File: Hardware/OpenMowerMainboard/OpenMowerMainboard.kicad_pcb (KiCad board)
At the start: 2 copper layers, 180 x 170 mm, 178 parts, among them IC1 74ALVC164245DGG,11, IC2 TSC101CILT, IC3 MAX20405AFOF_VY+T, J1 Conn_02x11_Top_Bottom, J10 Conn_01x05, J11 Conn_01x03_Male, J12 Conn_01x03_Male, J13 Conn_01x03_Male, J14 Conn_01x03_Male, J16 Conn_01x08, J17 Conn_01x02, J18 Conn_01x02, J19 Conn_01x04, J2 Conn_02x04_Top_Bottom, J20 Conn_01x10_Female, J21 Raspberry_Pi_2_3, J22 Conn_02x04_Odd_Even, J23 Conn_01x08, J3 Conn_01x02, J4 Conn_01x05, J5 Conn_01x04, J6 Conn_01x04, J7 Conn_01x04, J8 Conn_01x04, J9 Conn_01x04, M1 Fan, Q13 BSS138, Q14 BSS138, Q15 BSS138, Q16 BSS138, Q3 BSS138, Q5 BSS138, Q6 Q_PMOS_GDS, SW1 MK-11C04-G013, SW2 DA-01BP, U1 DNP, U10 74HC4051, U11 Pico, U2 MCP604, U3 SIP32509DT, U4 xESC2, U5 xESC2, U6 xESC2, U7 SN74LV1T34DBV, U9 74HC4051

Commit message: Initial mainboard for Worx Landroid WR105SI
Moved components and a few connectors around to make the mainboard fit
in the Worx Landroid WR105SI. No functional changes (hopefully).

Mounting holes are TBD.
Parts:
- removed H1: MountingHole_Pad, MountingHole:MountingHole_5mm_Pad_Via
- moved U1 160.3 mm to (187.9, 161.8), turned to 90 degrees
- moved LOGO1 160.1 mm to (163.5, 72.8)
- moved LOGO2 160.1 mm to (155.8, 72.5)
- moved H2 159.5 mm to (159.6, 94.7)
- moved J16 157.2 mm to (215.0, 69.4), turned to -90 degrees
- moved R7 152.0 mm to (212.7, 63.6)
- moved R13 147.8 mm to (210.1, 63.6)
- moved FID15 147.6 mm to (171.9, 165.3), turned to 90 degrees
- moved FID7 147.3 mm to (193.0, 138.8), turned to 90 degrees
- moved C10 147.0 mm to (183.0, 153.0), turned to -90 degrees
- moved J23 146.5 mm to (215.0, 75.0), turned to -90 degrees
- moved J20 140.6 mm to (198.1, 114.4), turned to 180 degrees
- moved D23 138.8 mm to (200.4, 83.8), turned to 0 degrees
- moved C19 138.0 mm to (188.4, 133.6), turned to 0 degrees
- moved C21 137.5 mm to (189.2, 131.2), turned to 0 degrees
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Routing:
- net /RobotConnectors/V_CHARGE: track 44.6 -> 267.5 mm
- net /RobotConnectors/V_BATTERY: track 31.3 -> 215.9 mm
- net /RobotConnectors/CHARGE_SHUNT_MINUS: track 82.0 -> 206.1 mm
- net /RobotConnectors/CHARGE_SHUNT_PLUS: track 80.0 -> 203.8 mm
- net /RobotConnectors/ENABLE_CHARGE: track 95.5 -> 216.1 mm, vias 2 -> 4
- net /ESCs/MR_TX: track 100.3 -> 194.9 mm
- net /ESCs/MR_RX: track 77.5 -> 171.2 mm
- net /pico/SOUND_BUSY: track 111.9 -> 24.4 mm, vias 3 -> 1
- net +5V: track 887.6 -> 970.6 mm, vias 18 -> 20
- net /IMU/SCK: track 205.5 -> 125.8 mm
- net /IMU/MOSI: track 202.0 -> 123.4 mm
- net /IMU/MISO: track 216.3 -> 138.8 mm
- net Net-(JP6-B): track 98.1 -> 169.3 mm, vias 5 -> 7
- net /IMU/~{CS}: track 186.9 -> 122.7 mm
- net /pico/SOUND_TX: track 107.9 -> 44.2 mm, vias 1 -> 3
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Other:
- board size 180 x 170 mm -> 257.1 x 170 mm

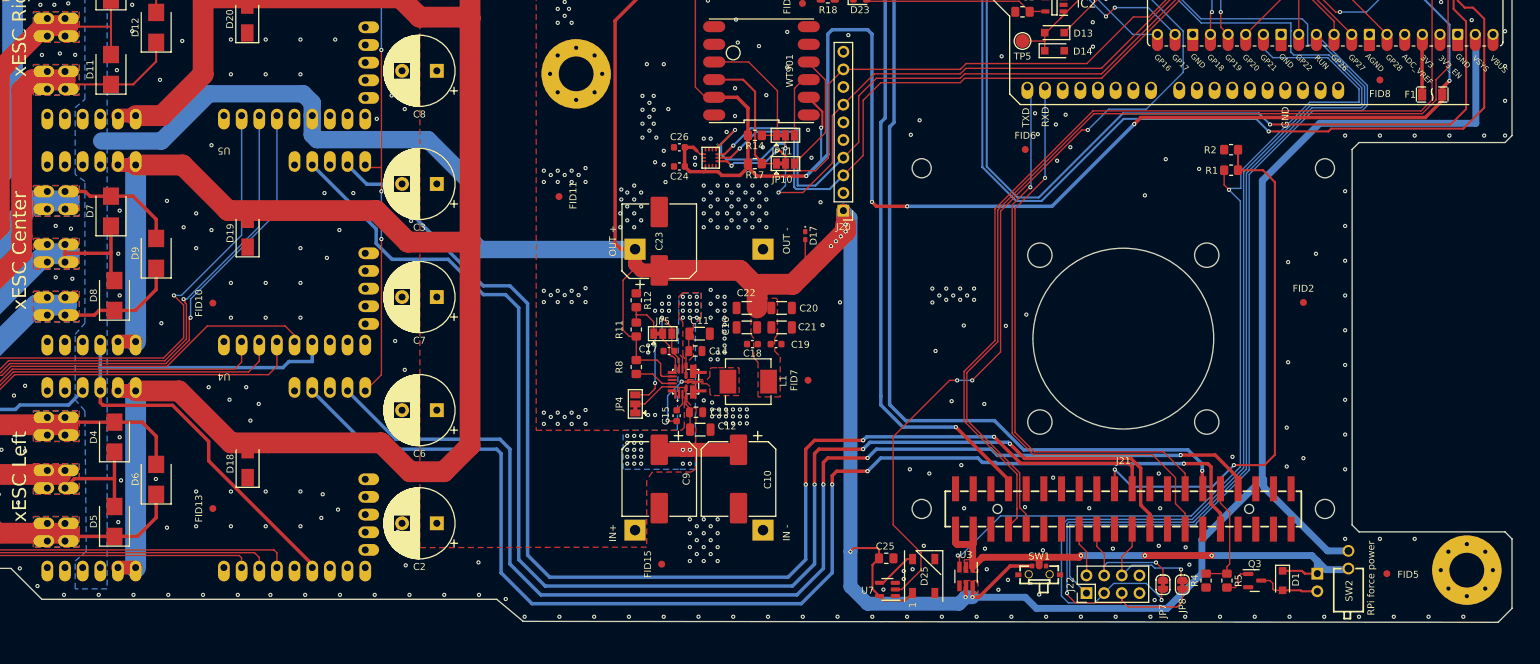
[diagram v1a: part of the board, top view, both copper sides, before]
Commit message: mainboard: squeeze bottom mid slightly
Slightly reduce board height near bottom mid. Should give a bit more
freedom when placing the board in the Landroid.
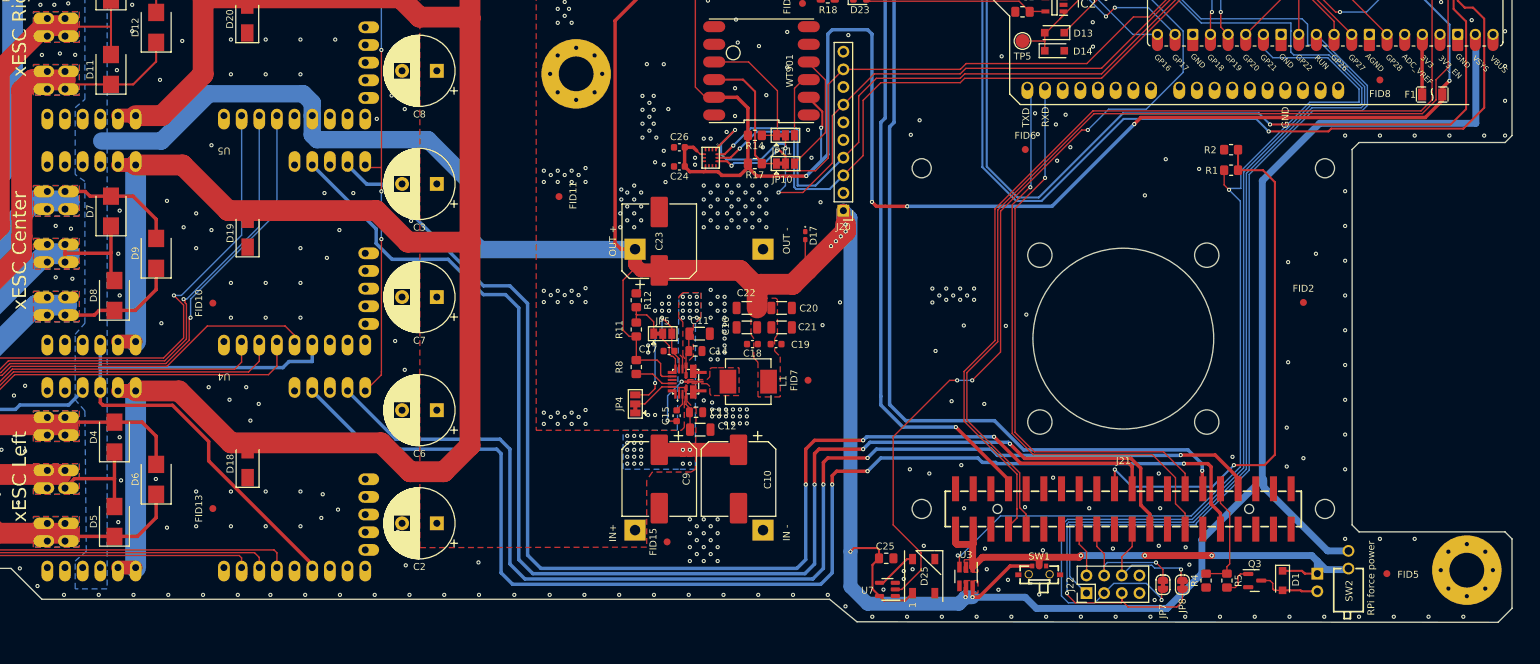
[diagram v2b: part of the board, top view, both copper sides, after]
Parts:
- moved FID15 3.30 mm to (172.7, 162.1)
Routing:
- net /ESCs/ML_RX: track 178.5 -> 176.2 mm
- net /ESCs/ML_TX: track 170.2 -> 168.3 mm
- net /ESCs/MC_RX: track 195.0 -> 193.5 mm
- net /ESCs/MC_TX: track 180.6 -> 179.6 mm
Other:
- outline, holes or cut-outs redrawn

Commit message: mainboard: no mounting holes, squeeze connectors
Remove mounting holes and squeeze upper right connectors
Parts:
- removed H2, H3, H4: MountingHole_Pad, MountingHole:MountingHole_5mm_Pad_Via
- moved FID11 27.3 mm to (171.0, 88.8)
- moved J5 12.7 mm to (266.7, 8.58)
- moved J6 12.7 mm to (266.7, 16.6)
- moved J11 10.8 mm to (282.1, 8.58)
- moved J12 10.8 mm to (282.1, 16.6)
- moved FID14 4.86 mm to (281.4, 24.4)
- moved C13 0.10 mm to (177.0, 143.4)
- moved C15 0.10 mm to (174.2, 143.9)
- moved C2 0.10 mm to (139.7, 159.3)
- moved C20 0.10 mm to (189.3, 128.4)
- moved C22 0.10 mm to (184.3, 128.4)
- moved D25 0.10 mm to (209.7, 166.9)
- moved J21 0.10 mm to (238.4, 157.3)
- moved JP7 0.10 mm to (244.1, 168.2)
- moved JP8 0.10 mm to (246.9, 168.2)
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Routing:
- net +5V: track 970.6 -> 1038.3 mm
- net /RobotConnectors/HALL_SWITCH_2_5V: track 50.3 -> 57.4 mm
- net /RobotConnectors/USS_3_ECHO_5V: track 50.6 -> 45.7 mm
- net /RobotConnectors/USS_4_ECHO_5V: track 42.5 -> 38.4 mm
- net /RobotConnectors/USS_5_ECHO_5V: track 34.9 -> 30.9 mm
- net /RobotConnectors/USS_2_TRIGGER_5V: track 68.7 -> 64.9 mm
- net /RobotConnectors/HALL_SWITCH_1_5V: track 62.1 -> 64.6 mm
- net /RobotConnectors/USS_1_TRIGGER_5V: track 77.4 -> 75.1 mm
- net /RobotConnectors/USS_1_ECHO_5V: track 65.5 -> 63.4 mm
- net /RobotConnectors/USS_2_ECHO_5V: track 57.5 -> 58.7 mm
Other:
- outline, holes or cut-outs redrawn

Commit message: mainboard: remove unused area in middle of board
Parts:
- moved LOGO2 55.5 mm to (167.4, 126.8), turned to 90 degrees
- moved LOGO1 47.6 mm to (167.6, 120.2), turned to -90 degrees
- moved FID13 18.3 mm to (125.2, 152.8)
- moved FID10 18.3 mm to (125.2, 123.3)
- moved FID12 18.3 mm to (90.2, 108.8)
- moved Q5 18.3 mm to (90.5, 75.2)
- moved D20 18.3 mm to (130.2, 82.5)
- moved Q6 18.3 mm to (86.5, 81.5)
- moved R26 18.3 mm to (95.5, 75.2)
- moved D2 18.3 mm to (81.2, 73.0)
- moved F2 18.3 mm to (66.4, 93.0)
- moved F4 18.3 mm to (66.4, 84.9)
- moved FID16 18.3 mm to (75.2, 73.2)
- moved D3 18.3 mm to (81.2, 69.2)
- moved D4 18.3 mm to (111.0, 142.6)
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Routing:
- net +5V: track 1038.3 -> 1025.8 mm
- net /ESCs/ML_RX: track 176.2 -> 165.5 mm
- net Net-(JP6-B): track 169.3 -> 159.3 mm
- net /RobotConnectors/V_BATTERY: track 215.9 -> 205.9 mm
- net /ESCs/MR_RX: track 171.2 -> 161.2 mm
- net /RobotConnectors/V_CHARGE: track 267.5 -> 257.5 mm
- net /RobotConnectors/CHARGE_SHUNT_MINUS: track 206.1 -> 196.1 mm
- net /RobotConnectors/CHARGE_SHUNT_PLUS: track 203.8 -> 193.8 mm
- net /RobotConnectors/ENABLE_CHARGE: track 216.1 -> 206.1 mm
- net /ESCs/MR_TX: track 194.9 -> 184.9 mm
- net /ESCs/ML_TX: track 168.3 -> 158.4 mm
- net /ESCs/MC_RX: track 193.5 -> 185.1 mm
- net /ESCs/MC_TX: track 179.6 -> 171.2 mm
- net GND: vias 595 -> 589
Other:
- board size 257.1 x 170 mm -> 247.1 x 170 mm
